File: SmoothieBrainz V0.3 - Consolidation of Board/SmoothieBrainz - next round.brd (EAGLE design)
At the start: 101 x 101 mm, 217 parts, among them IC1 LPC1769, IC5 LD117ADT33TR, Q1 BSL207SP, Q2 12MHz, SW1 SW_TACT_4P_B, SW3 SW_TACT_4P_B, U3 USD-SOCKETUSD, X1 MSTBA2, X14 USBPTH, X2 GMSTBA2, X3 GMSTBA4, X4 1751248, X5 1751248, X6 1751248, X7 1751248

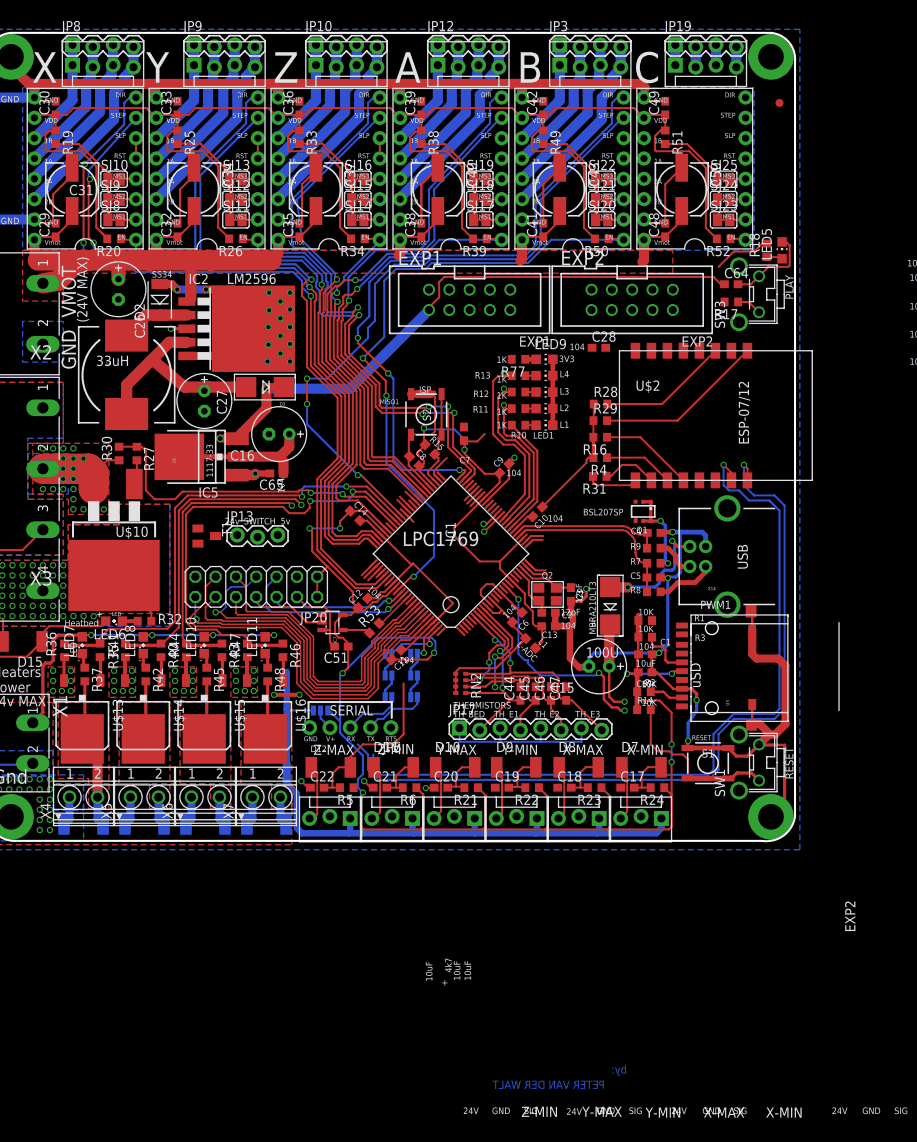
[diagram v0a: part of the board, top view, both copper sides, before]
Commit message: mosfet6 circuit complete, lots more routing
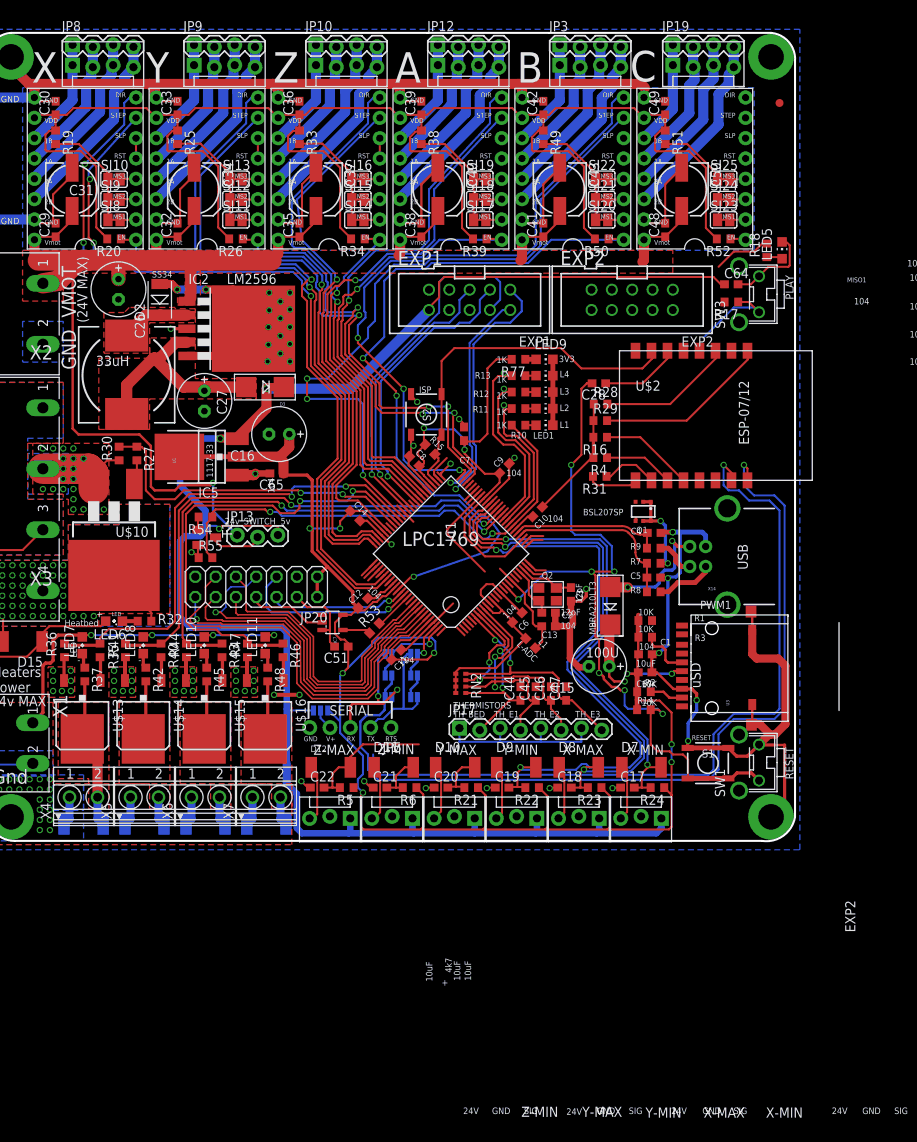
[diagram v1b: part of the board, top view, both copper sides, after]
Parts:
- added R54: 10r, resistor:R0603
- added R55: 100k, resistor:R0603
- C28: value .1uF -> 104
- RN2: value (none) -> 4k7
- T1: value (none) -> BC817
- moved C28 4.45 mm to (76.5, 57.2), turned to 180 degrees
- moved JP18 0.32 mm to (85.7, 96.8)
- moved JP19 0.32 mm to (85.7, 99.4)
- moved T1 0.16 mm to (27.5, 37.9)
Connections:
- new net N$55: R54.2, T1.B
- new net N$56: JP13.2, T1.C
- net 24V: now also JP13.1
- net 5V: now also JP13.3
- net GND: now also R55.1, T1.E
- net LED1: now also R54.1, R55.2
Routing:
- net Y_MIN: track 7.03 -> 79.3 mm, vias 0 -> 2
- net X_MAX: track 7.03 -> 70.4 mm, vias 0 -> 2
- net 5V: track 168.3 -> 225.1 mm, vias 3 -> 4
- net X_MIN: track 7.12 -> 62.5 mm, vias 0 -> 2
- net 24V: track 104.5 -> 156.7 mm, vias 0 -> 1
- net LED1: track 15.4 -> 61.8 mm, vias 0 -> 2
- net SSEL1: track 1.77 -> 46.0 mm, vias 0 -> 1
- net RESET: track 49.2 -> 92.6 mm, vias 3 -> 7
- net MOSI1: track 1.78 -> 36.4 mm, vias 0 -> 1
- net ISP_BOOT: track 12.4 -> 46.2 mm
- net SCK1: track 1.83 -> 34.9 mm, vias 0 -> 1
- net BUZZER-RRD: track 0.00 -> 30.3 mm, vias 0 -> 1
- net P1_22-3RD-SMALL-FET: track 38.4 -> 65.8 mm
- net P1_30_CLICK-ON-RRD: track 0.00 -> 26.0 mm, vias 0 -> 1
- net P1_23-3RD-LARGE-FET: track 40.3 -> 66.1 mm
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- added copper zone on layer 1, net 5VREG
- added copper zone on layer 1, net N$9
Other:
- board text added: "Based on work from:"
- board text added: "Derived from:"
- board text added: "github.com/openhardwarecoza"
- board text removed: "PETER VAN DER WALT"
- board text removed: "by:"

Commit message: ran auto for some sanity
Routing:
- net SD_MISO: track 6.31 -> 153.3 mm, vias 0 -> 3
- net SD_SCK: track 1.96 -> 139.7 mm, vias 0 -> 3
- net PLAY_LED: track 8.13 -> 124.6 mm, vias 0 -> 4
- net SD-CD-ON-RRD: track 2.47 -> 106.3 mm, vias 0 -> 1
- net SD_MOSI: track 8.44 -> 109.8 mm, vias 0 -> 6
- net RTS: track 11.8 -> 111.6 mm, vias 0 -> 2
- net 3.3V: track 538.9 -> 619.1 mm
- net Z_MIN: track 8.21 -> 75.4 mm, vias 0 -> 4
- net SD_CS: track 0.95 -> 67.4 mm, vias 0 -> 4
- net PLAY: track 14.0 -> 72.0 mm, vias 1 -> 3
- net P2.9: track 2.86 -> 59.0 mm, vias 0 -> 4
- net LED2: track 19.6 -> 72.4 mm
- net LED3: track 21.3 -> 70.2 mm
- net GND: track 486.3 -> 533.5 mm, vias 91 -> 92
- net SD_IRQ-ENC-A-ON-RRD: track 2.42 -> 48.4 mm, vias 0 -> 3
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
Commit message: Revert "ran auto for some sanity"
This reverts commit 1ed6ee52647e90fc58e62b905c32a851aa249b6f.
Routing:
- net SD_MISO: track 153.3 -> 6.31 mm, vias 3 -> 0
- net SD_SCK: track 139.7 -> 1.96 mm, vias 3 -> 0
- net PLAY_LED: track 124.6 -> 8.13 mm, vias 4 -> 0
- net SD-CD-ON-RRD: track 106.3 -> 2.47 mm, vias 1 -> 0
- net SD_MOSI: track 109.8 -> 8.44 mm, vias 6 -> 0
- net RTS: track 111.6 -> 11.8 mm, vias 2 -> 0
- net 3.3V: track 619.1 -> 538.9 mm
- net Z_MIN: track 75.4 -> 8.21 mm, vias 4 -> 0
- net SD_CS: track 67.4 -> 0.95 mm, vias 4 -> 0
- net PLAY: track 72.0 -> 14.0 mm, vias 3 -> 1
- net P2.9: track 59.0 -> 2.86 mm, vias 4 -> 0
- net LED2: track 72.4 -> 19.6 mm
- net LED3: track 70.2 -> 21.3 mm
- net GND: track 533.5 -> 486.3 mm, vias 92 -> 91
- net SD_IRQ-ENC-A-ON-RRD: track 48.4 -> 2.42 mm, vias 3 -> 0
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
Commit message: BOM-0
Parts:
- removed U$11: FIDUCIAL, adafruit:FIDUCIAL_1MM
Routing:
- net 5VREG: track 26.9 -> 26.2 mm
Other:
- board text removed: "220U"
- board text removed: "22R"
- board text removed: "24V"
- board text removed: "4k7"
- board text removed: "5V"
- board text removed: "74LVC1G04"
- board text removed: "DIR1"
- board text removed: "DIR2"
- board text removed: "DIR3"
- board text removed: "DIR4"
- board text removed: "DIR5"
- board text removed: "Derived from:"
- board text removed: "EN/CS1"
- board text removed: "EN/CS2"
- board text removed: "EN/CS3"
- board text removed: "EN/CS4"
- board text removed: "EN/CS5"
- board text removed: "LASER / CNC / 3D-PRINT"
- board text removed: "MISO"
- board text removed: "MISO1"
- board text removed: "MOSI"
- board text removed: "P1.22"
- board text removed: "P1.23"
- board text removed: "P2.6"
- board text removed: "P2.7"
- board text removed: "PWM0"
- board text removed: "SCK"
- board text removed: "SIG"
- board text removed: "STEP1"
- board text removed: "STEP2"
- board text removed: "STEP3"
- board text removed: "STEP4"
- board text removed: "STEP5"

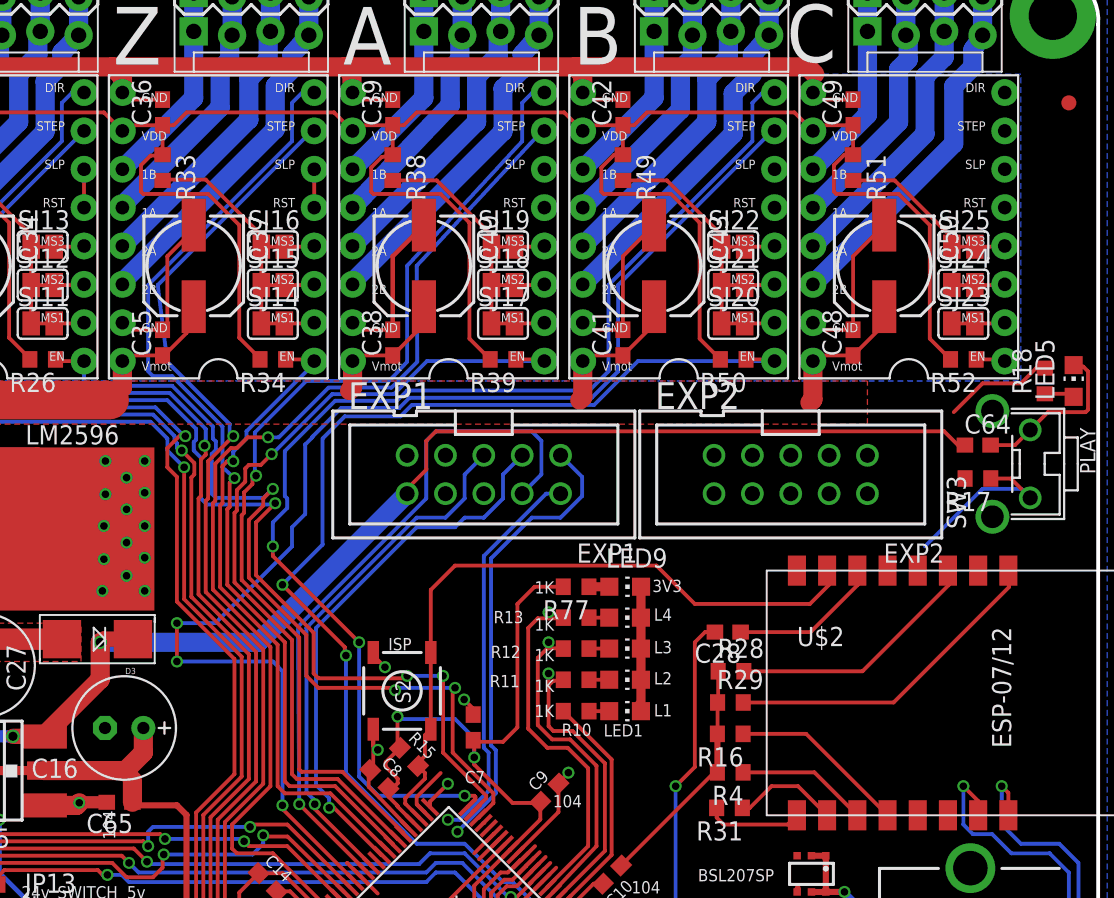
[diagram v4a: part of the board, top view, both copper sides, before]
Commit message: routed motor 6, some lcd traces
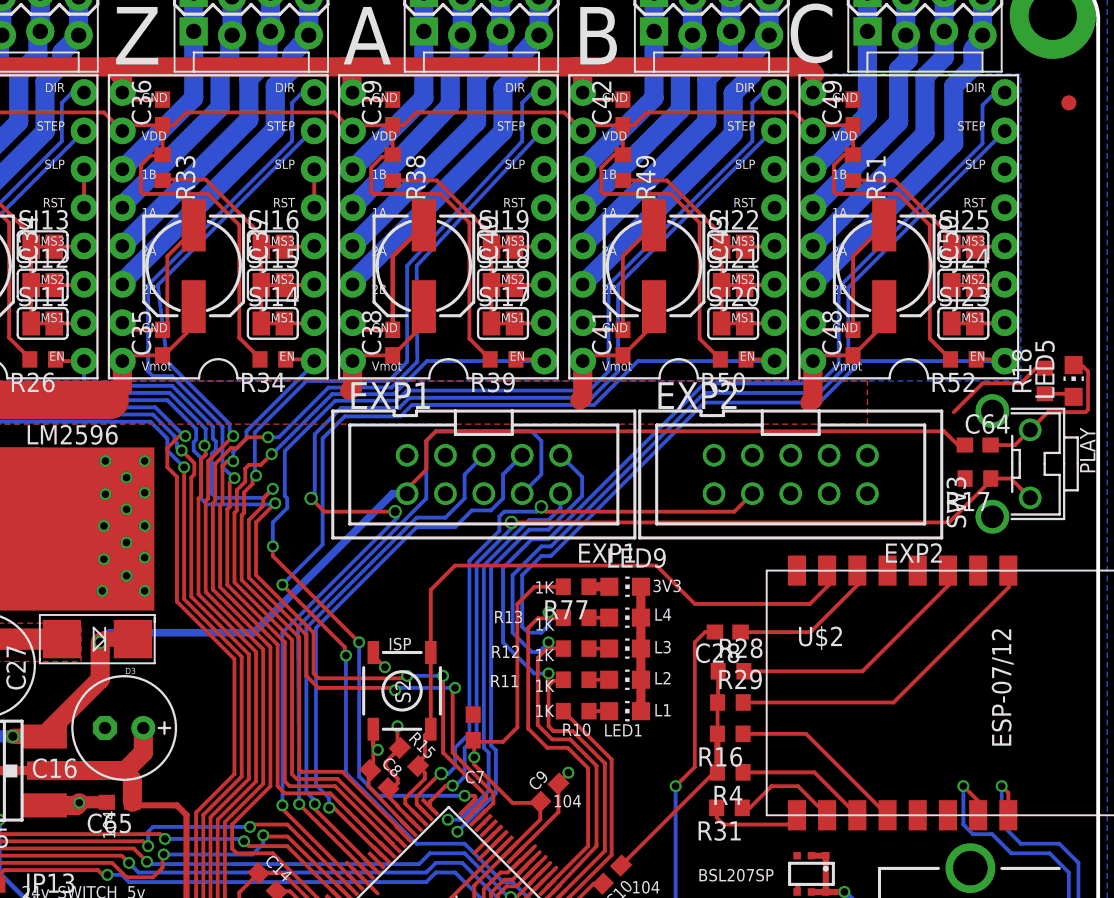
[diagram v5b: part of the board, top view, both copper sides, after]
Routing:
- net LED2: track 19.6 -> 79.1 mm
- net LED3: track 21.3 -> 76.1 mm
- net PLAY: track 14.0 -> 58.5 mm, vias 1 -> 2
- net LED4: track 25.6 -> 69.9 mm
- net SD_CD/KILL-ON-RRD: track 3.48 -> 40.0 mm, vias 0 -> 2
- net 3.3V: track 538.9 -> 531.4 mm
- net STP5: track 85.7 -> 82.1 mm
- net GND: track 486.3 -> 485.5 mm, vias 91 -> 90

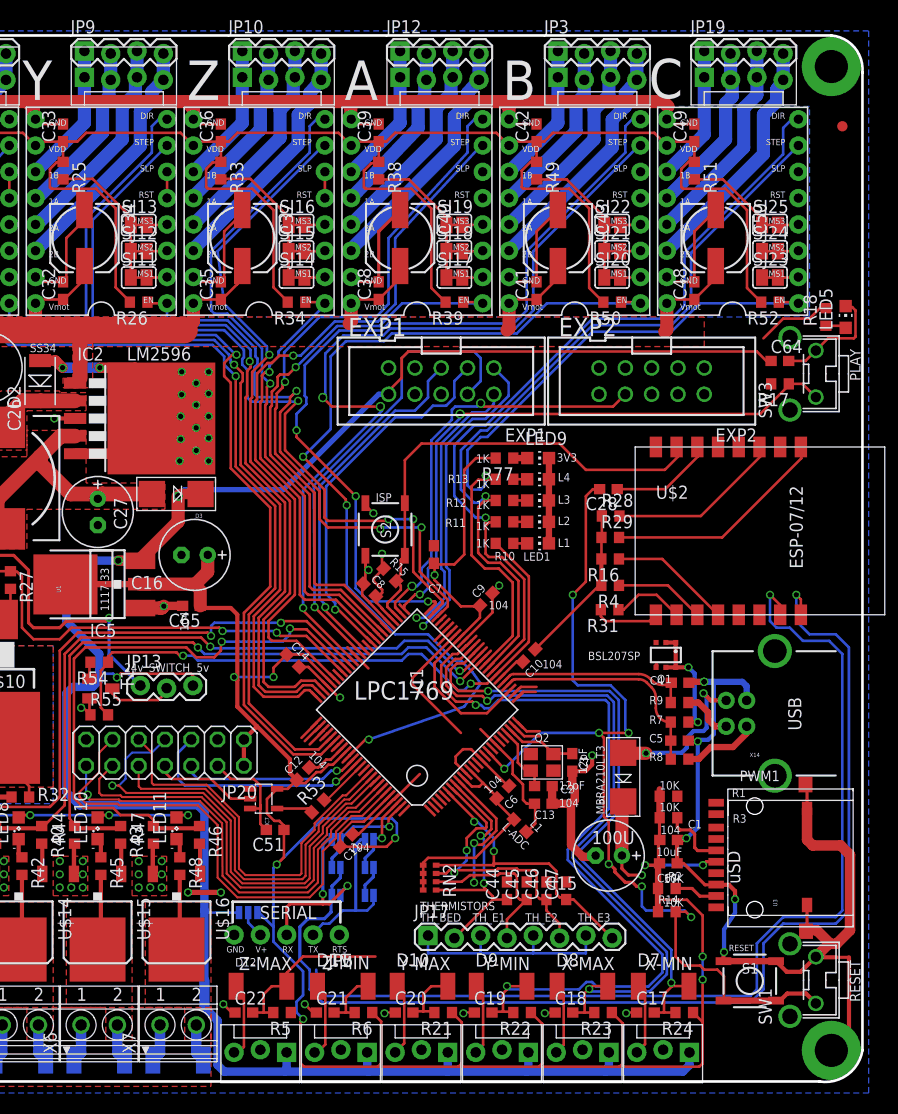
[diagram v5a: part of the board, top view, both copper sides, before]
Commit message: insufficient gnd for motors
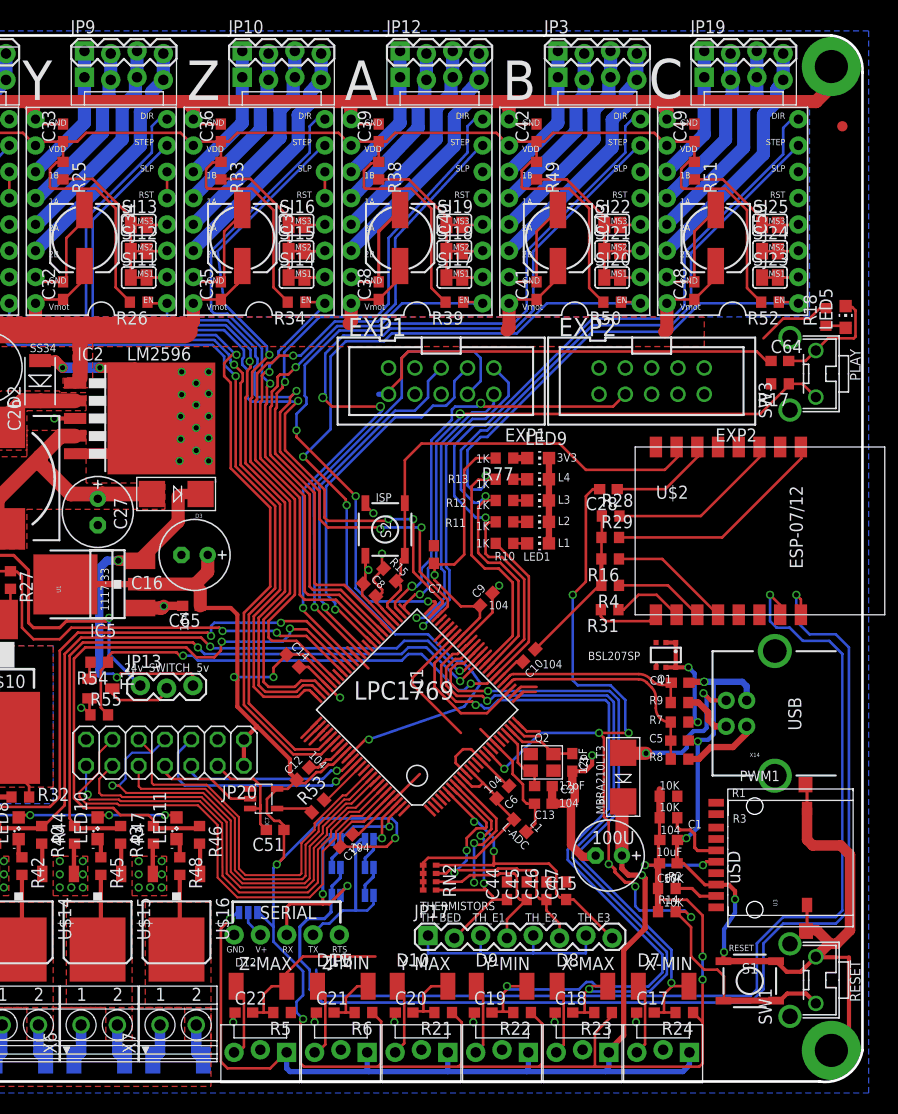
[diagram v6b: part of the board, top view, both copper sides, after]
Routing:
- net 5V: track 225.1 -> 175.6 mm
- net GND: track 485.5 -> 501.6 mm, vias 90 -> 88
- net HEATERVIN: track 59.6 -> 57.9 mm
- net RESET: track 92.6 -> 92.0 mm

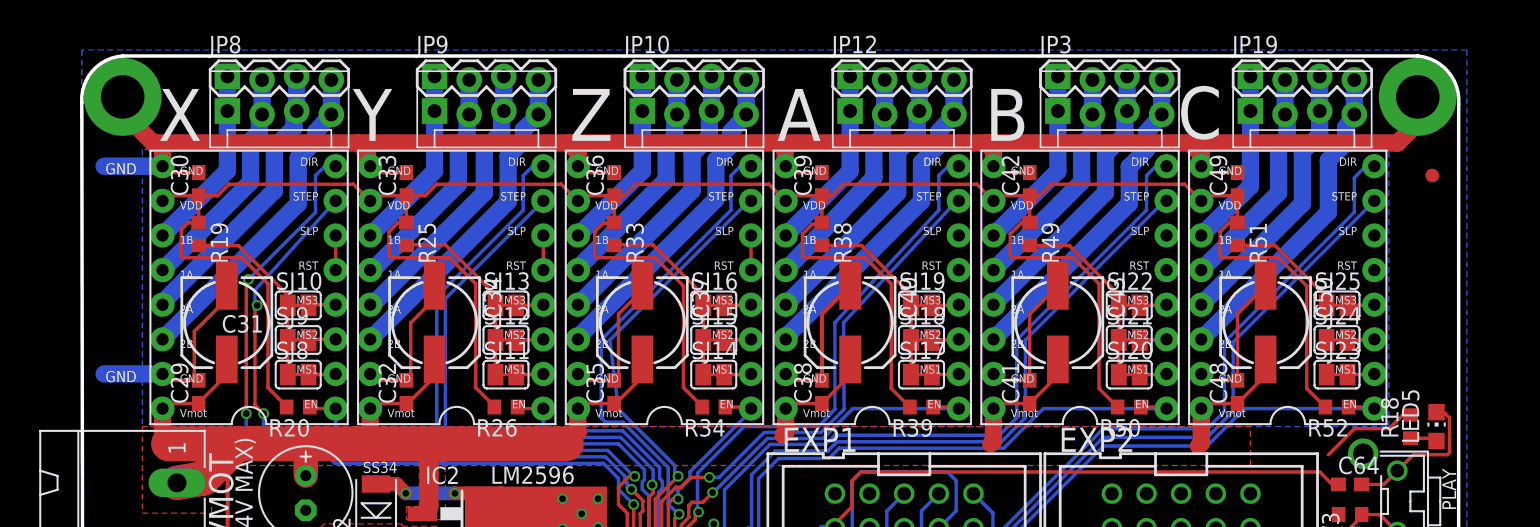
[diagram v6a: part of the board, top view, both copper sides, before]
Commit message: Major rework of Y motor driver layout and increased gnd planes
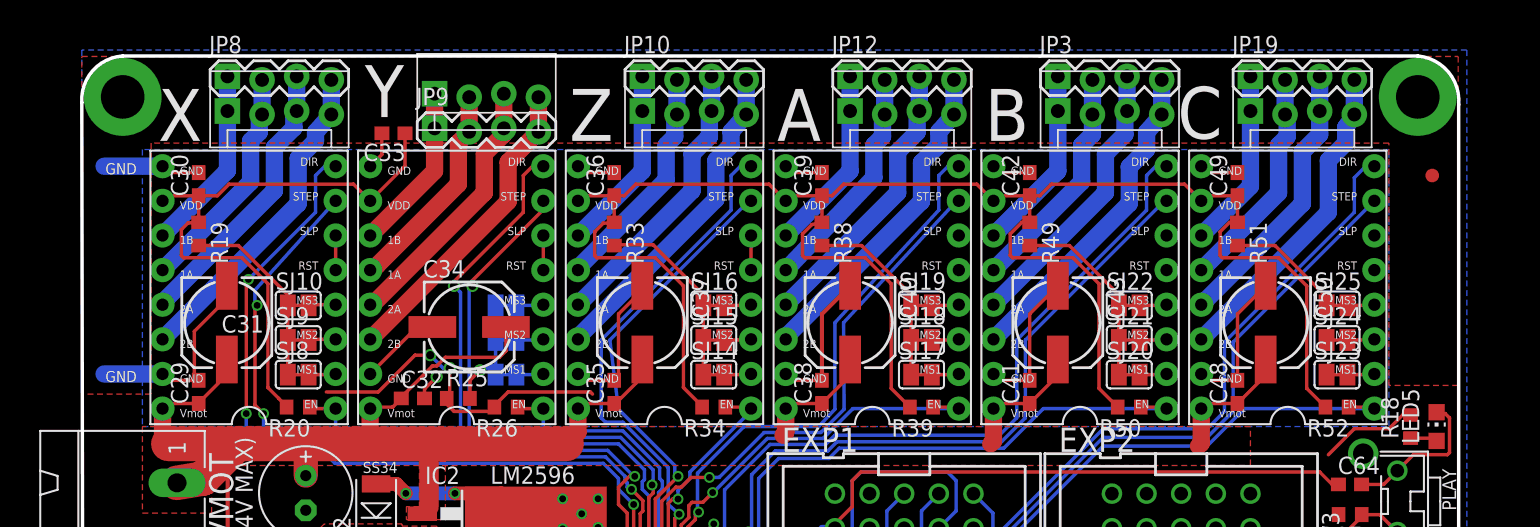
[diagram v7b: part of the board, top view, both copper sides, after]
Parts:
- moved R25 12.7 mm to (27.6, 75.9), turned to 0 degrees
- moved C33 3.85 mm to (22.9, 95.3), turned to 180 degrees
- moved JP9 3.81 mm to (25.9, 95.6)
- moved C34 2.56 mm to (28.4, 81.1), turned to 0 degrees
- moved JP2 1.27 mm to (25.9, 98.1)
- moved C32 0.67 mm to (24.3, 75.9), turned to 0 degrees
- flipped SJ11 to the bottom, turned to 180 degrees
- flipped SJ12 to the bottom, turned to 180 degrees
- flipped SJ13 to the bottom, turned to 180 degrees
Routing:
- net GND: track 501.6 -> 388.5 mm, vias 88 -> 89
- net 3.3V: track 531.5 -> 523.2 mm, vias 11 -> 13
- net 24V: track 156.7 -> 163.5 mm
- net N$14: track 13.9 -> 9.00 mm, vias 0 -> 1
- net STP2: track 78.4 -> 75.9 mm, vias 1 -> 2
- net DIR2: track 82.4 -> 80.3 mm, vias 3 -> 4
- net 2A2M: track 21.0 -> 19.6 mm
- net 1A2M: track 17.1 -> 15.8 mm
- net 1B2M: track 13.6 -> 12.4 mm
- net 2B2M: track 24.1 -> 22.9 mm
